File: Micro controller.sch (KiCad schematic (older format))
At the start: 31 parts, among them J1 USB_B, U1 BAT54C, U14 ferrite, U20 TPD3S014, U21 MKL02Z32VFG4, U22 LP38691, U23 MK66FX1M0, U3 ferrite, U5 ferrite, U6 BAT54C, Y1 Crystal_16MHz, Y2 32.768MHz

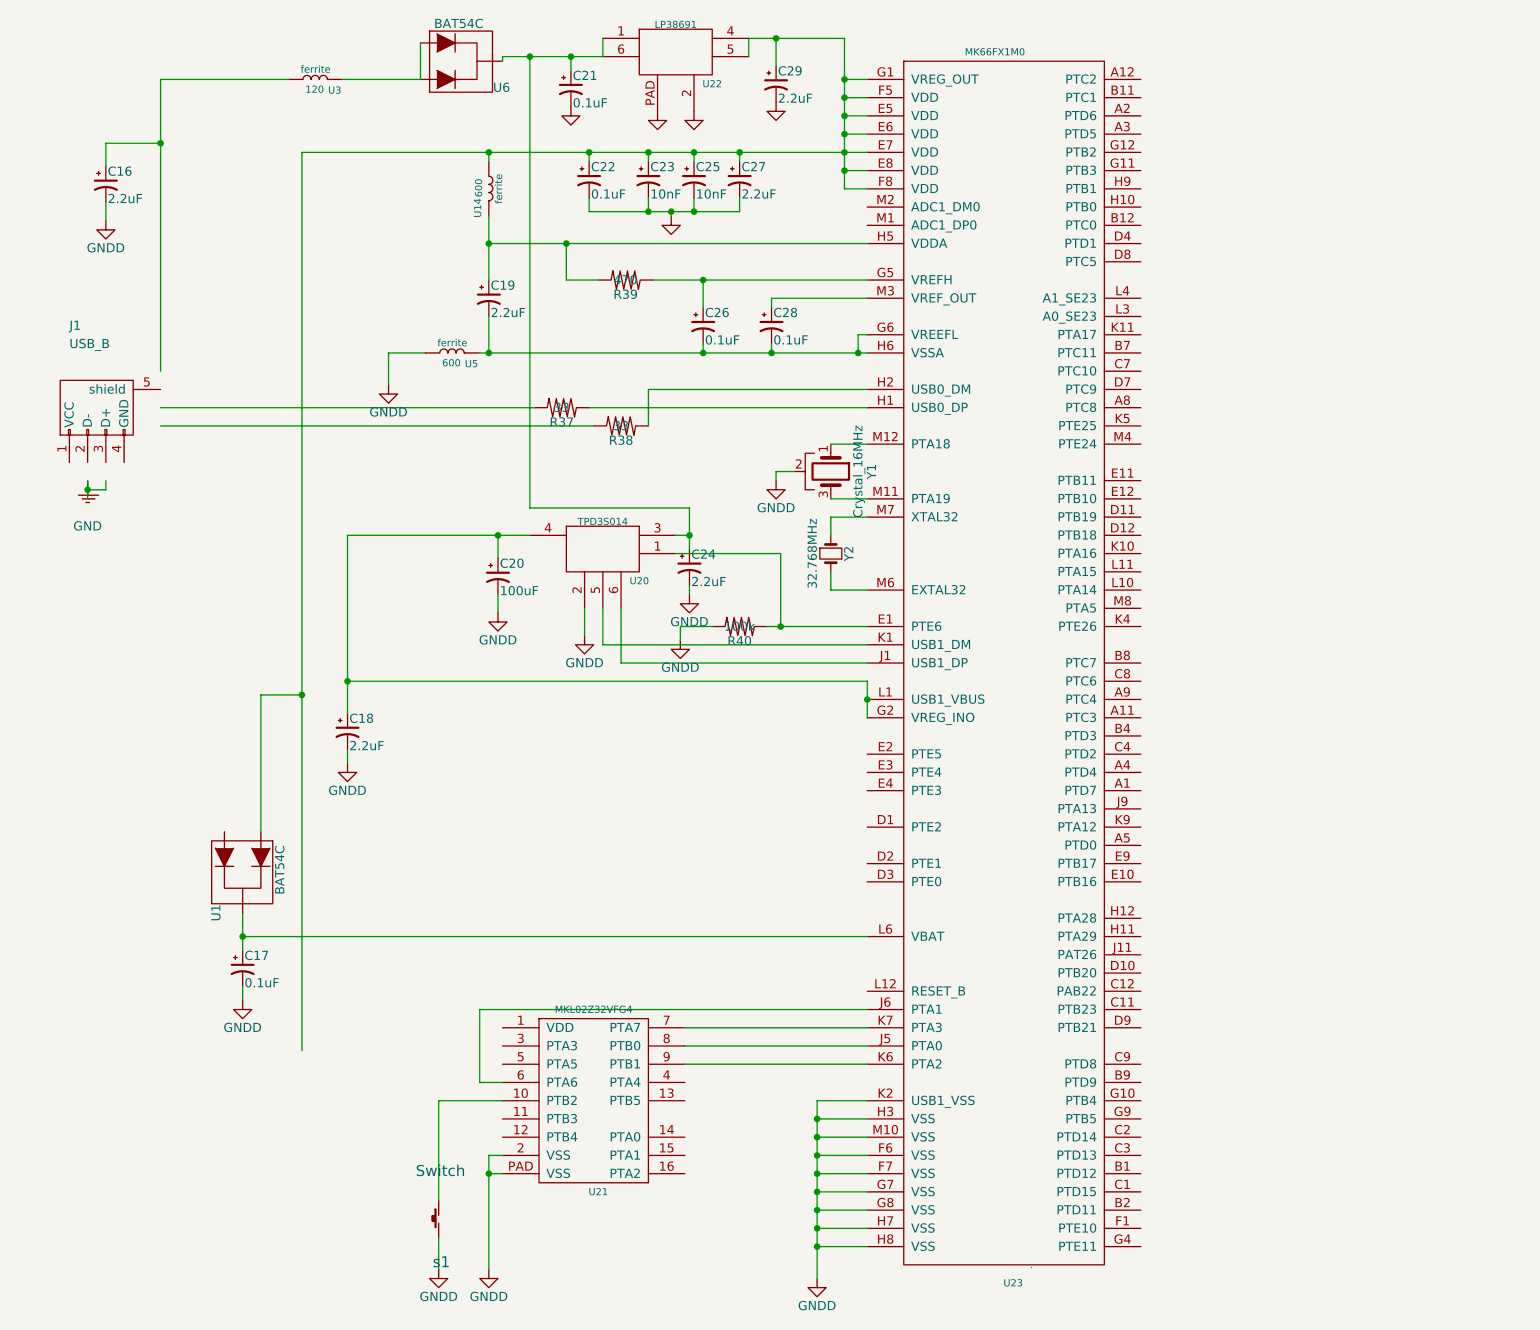
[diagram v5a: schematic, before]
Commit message: added TPS61222DCK boost converter
-added TPS61222DCK boost converter for 5V input of the encoder
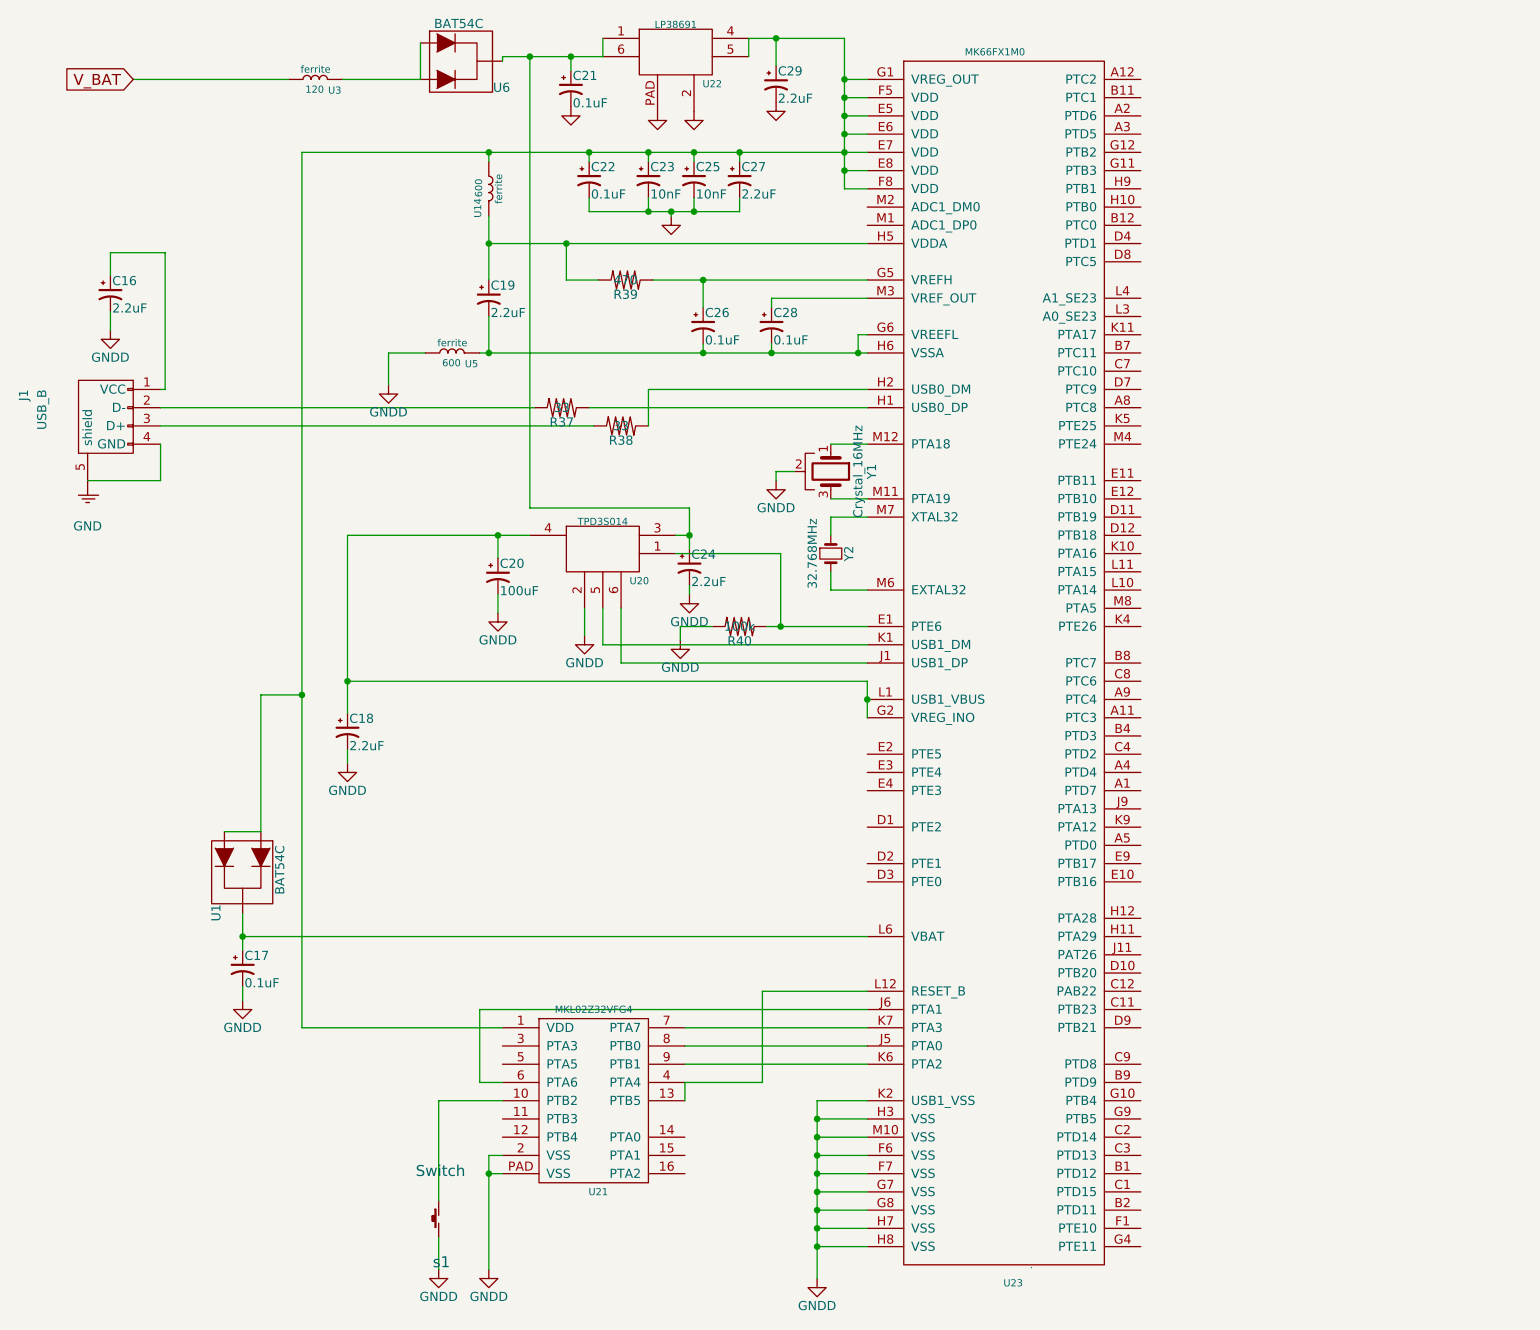
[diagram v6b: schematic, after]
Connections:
- net labels added: V_BAT
- wire segments 115 -> 121
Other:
- moved on the sheet: C16, J1
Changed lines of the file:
@@
 L USB_B J1
 U 1 1 59498F09
-P 1000 2625
-F 0 "J1" H 800 3075 50  0000 L CNN
-F 1 "USB_B" H 800 2975 50  0000 L CNN
-F 2 "micromouse:USB_Micro-B" H 1150 2575 50  0001 C CNN
-F 3 "" H 1150 2575 50  0001 C CNN
-	1    1000 2625
-	1    0    0    -1
+P 1000 2725
+F 0 "J1" H 800 3175 50  0000 L CNN
+F 1 "USB_B" H 800 3075 50  0000 L CNN
+F 2 "micromouse:USB_Micro-B" H 1150 2675 50  0001 C CNN
+F 3 "" H 1150 2675 50  0001 C CNN
+	1    1000 2725
+	0    -1   1    0
 $EndComp
 $Comp
@@
 L CP1_Small C16
 U 1 1 594A0EDA
-P 1000 1400
-F 0 "C16" H 1010 1470 50  0000 L CNN
-F 1 "2.2uF" H 1010 1320 50  0000 L CNN
-F 2 "micromouse:C_0603" H 1000 1400 50  0001 C CNN
-F 3 "" H 1000 1400 50  0001 C CNN
-	1    1000 1400
+P 1025 2000
+F 0 "C16" H 1035 2070 50  0000 L CNN
+F 1 "2.2uF" H 1035 1920 50  0000 L CNN
+F 2 "micromouse:C_0603" H 1025 2000 50  0001 C CNN
+F 3 "" H 1025 2000 50  0001 C CNN
+	1    1025 2000
 	1    0    0    -1
 $EndComp
@@
 L GNDD #PWR028
 U 1 1 594A0F24
-P 1000 1600
-F 0 "#PWR028" H 1000 1350 50  0001 C CNN
-F 1 "GNDD" H 1000 1450 50  0000 C CNN
-F 2 "" H 1000 1600 50  0001 C CNN
-F 3 "" H 1000 1600 50  0001 C CNN
-	1    1000 1600
+P 1025 2200
+F 0 "#PWR028" H 1025 1950 50  0001 C CNN
+F 1 "GNDD" H 1025 2050 50  0000 C CNN
+F 2 "" H 1025 2200 50  0001 C CNN
+F 3 "" H 1025 2200 50  0001 C CNN
+	1    1025 2200
 	1    0    0    -1
 $EndComp
@@
 $EndComp
 $Comp
-L GND #PWR28
-U 1 1 594A1F04
-P 900 3125
-F 0 "#PWR28" H 900 2875 50  0001 C CNN
-F 1 "GND" H 900 2975 50  0000 C CNN
-F 2 "" H 900 3125 50  0001 C CNN
-F 3 "" H 900 3125 50  0001 C CNN
-	1    900  3125
-	1    0    0    -1
-$EndComp
-$Comp
 L R R38
 U 1 1 594A207F
@@
 	2725 625  2725 825
 Wire Wire Line
-	1300 825  1300 2425
-Wire Wire Line
-	1000 1600 1000 1500
-Wire Wire Line
-	1000 1300 1000 1175
-Wire Wire Line
-	1000 1175 1300 1175
-Connection ~ 1300 1175
+	1025 2200 1025 2100
+Wire Wire Line
+	1025 1900 1025 1775
+Wire Wire Line
+	1025 1775 1325 1775
 Wire Wire Line
 	2075 1225 5175 1225
@@
 	2725 825  2300 825
 Wire Wire Line
-	2000 825  1300 825
-Wire Wire Line
-	900  3125 900  3025
-Wire Wire Line
-	1000 3025 1000 3075
-Wire Wire Line
-	1000 3075 900  3075
-Connection ~ 900  3075
-Wire Wire Line
 	5175 2625 3650 2625
 Wire Wire Line
@@
 Wire Wire Line
 	3675 2725 1300 2725
-Wire Wire Line
-	2075 1225 2075 6150
 Connection ~ 3100 1225
 Connection ~ 2075 4200
@@
 	1    0    0    -1
 $EndComp
+$Comp
+L GND #PWR28
+U 1 1 594A1F04
+P 900 3125
+F 0 "#PWR28" H 900 2875 50  0001 C CNN
+F 1 "GND" H 900 2975 50  0000 C CNN
+F 2 "" H 900 3125 50  0001 C CNN
+F 3 "" H 900 3125 50  0001 C CNN
+	1    900  3125
+	1    0    0    -1
+$EndComp
+Wire Wire Line
+	1300 2825 1300 3025
+Wire Wire Line
+	1300 3025 900  3025
+Wire Wire Line
+	1325 1775 1325 2525
+Wire Wire Line
+	1325 2525 1300 2525
+Text GLabel 1150 825  0    60   Input ~ 0
+V_BAT
+Wire Wire Line
+	2000 825  1150 825
+Wire Wire Line
+	2075 1225 2075 6025
+Wire Wire Line
+	2075 6025 3175 6025
+Wire Wire Line
+	1850 4950 1650 4950
+Wire Wire Line
+	4175 6425 4175 6325
+Wire Wire Line
+	4175 6325 4600 6325
+Wire Wire Line
+	4600 6325 4600 5825
+Wire Wire Line
+	4600 5825 5175 5825
 $EndSCHEMATC
